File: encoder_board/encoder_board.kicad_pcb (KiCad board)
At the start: 2 copper layers, 42 x 16 mm, 8 parts, among them J1 Conn_01x06, U1 AS5048A

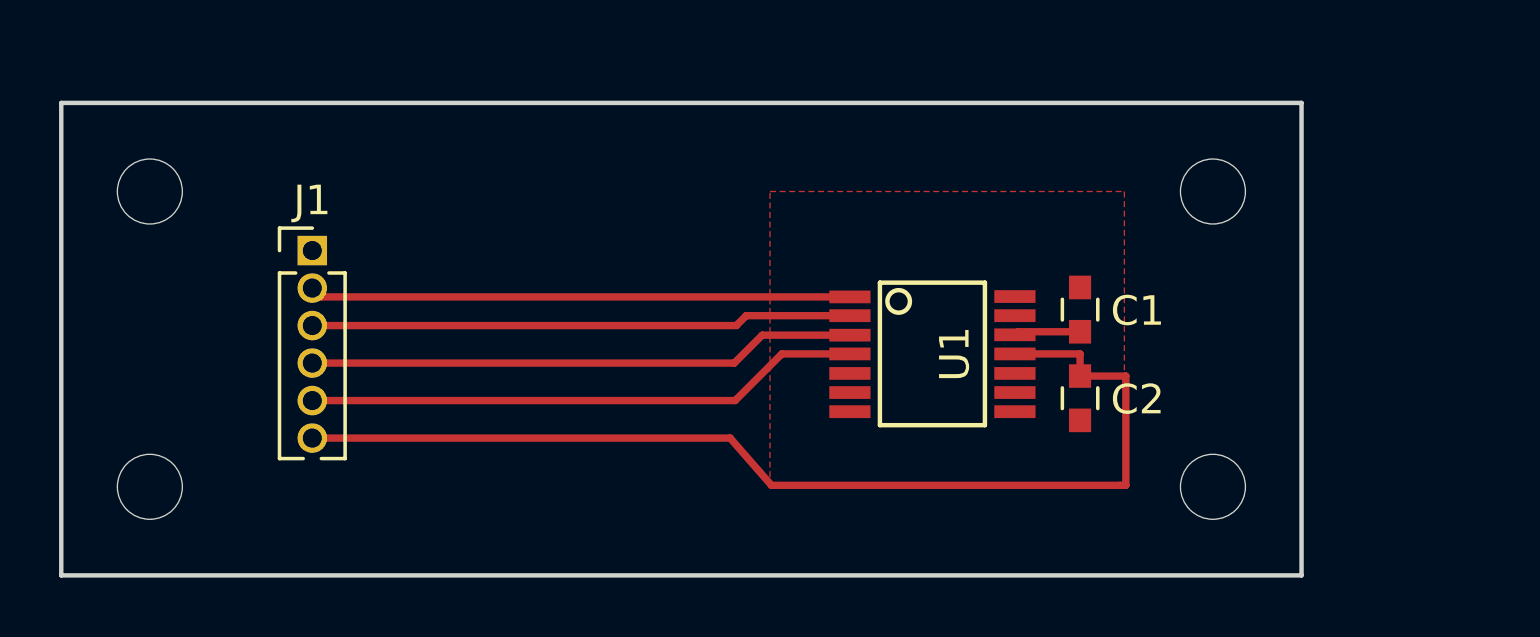
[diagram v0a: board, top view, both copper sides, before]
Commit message: add footprint for small ir sensors
 - use 0402 in encoder board
 - still need to switch sensor board
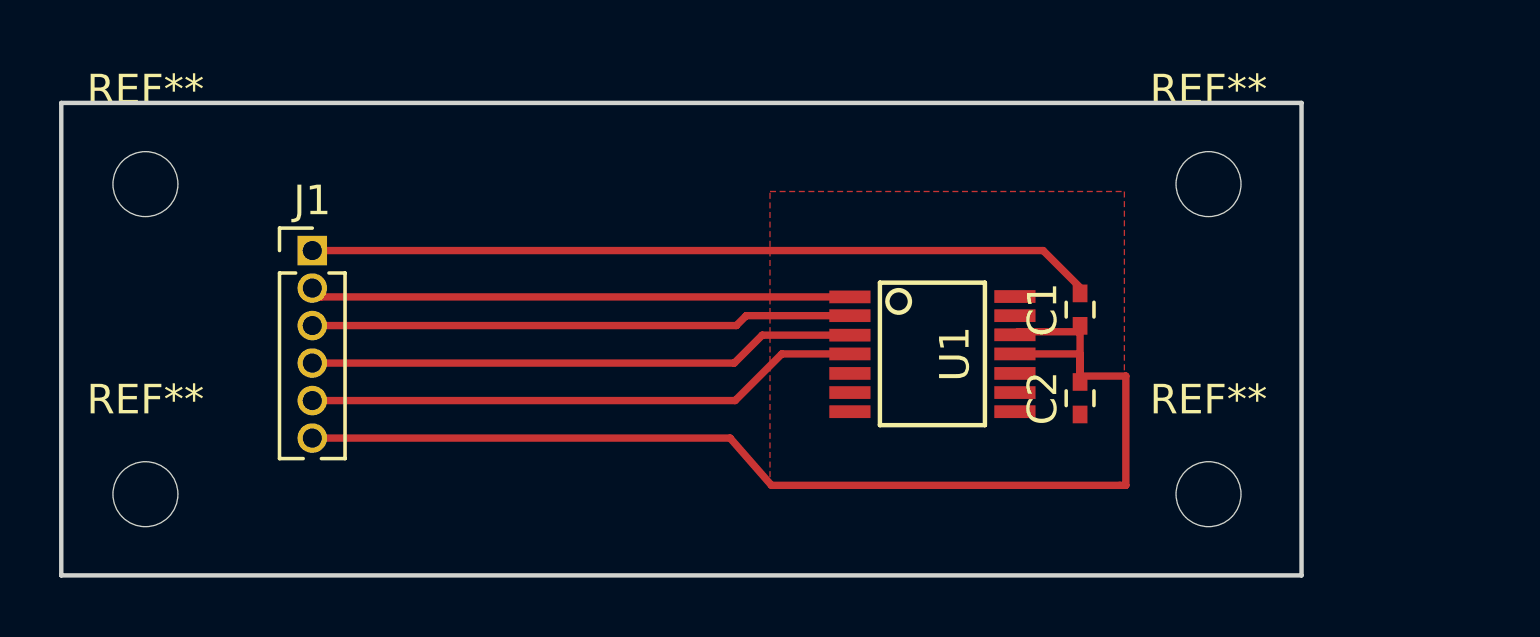
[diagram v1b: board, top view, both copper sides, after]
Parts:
- removed the REF** at (139.0, 103.0)
- removed the REF** at (139.0, 113.0)
- removed the REF** at (103.0, 103.0)
- removed the REF** at (103.0, 113.0)
- added REF**: MountingHole_2.2mm_M2, Mounting_Holes:MountingHole_2.2mm_M2, F.Cu at (102.8, 102.8)
- added REF**: MountingHole_2.2mm_M2, Mounting_Holes:MountingHole_2.2mm_M2, F.Cu at (102.8, 113.2)
- added REF**: MountingHole_2.2mm_M2, Mounting_Holes:MountingHole_2.2mm_M2, F.Cu at (138.8, 113.2)
- added REF**: MountingHole_2.2mm_M2, Mounting_Holes:MountingHole_2.2mm_M2, F.Cu at (138.8, 102.8)
- C1, C2: footprint Capacitors_SMD:C_0603 -> Capacitors_SMD:C_0402
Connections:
- C1 pad 1: Net-(C1-Pad1) -> +3V3
- C2 pad 2: +5V -> +3V3
- J1 pad 6: +5V -> +3V3
- U1 pad 11: +5V -> +3V3
- U1 pad 12: Net-(C1-Pad1) -> +3V3
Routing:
- net +3V3: track 0.00 -> 40.4 mm
- net +5V: track 36.5 -> 0.00 mm
- net GND: track 0.00 -> 26.5 mm
- net Net-(C1-Pad1): track 2.25 -> 0.00 mm

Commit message: fix grid origin and tweaked placement
 - added nice dimension indicators
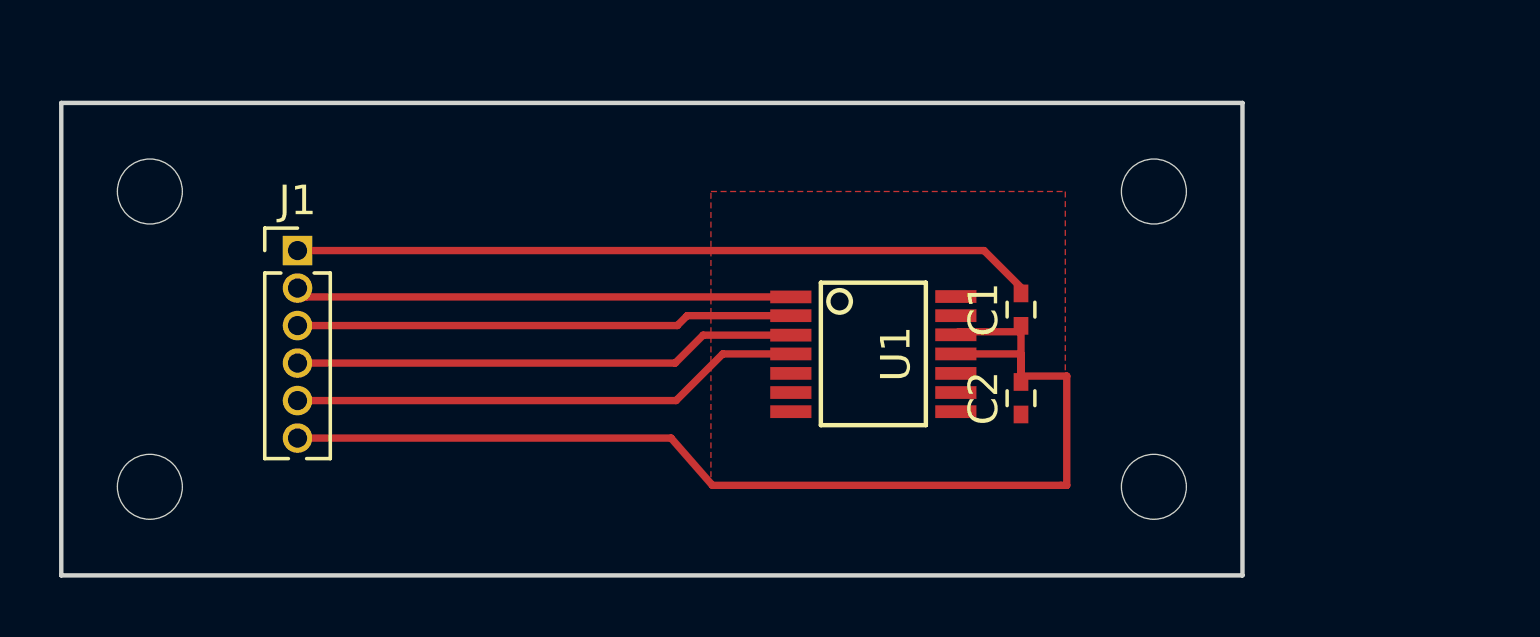
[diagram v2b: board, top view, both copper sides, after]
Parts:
- moved C1 2.00 mm to (132.5, 107.0)
- moved C2 2.00 mm to (132.5, 110.0)
- moved U1 2.00 mm to (127.5, 108.5)
- moved REF** 1.87 mm to (137.0, 113.0)
- moved REF** 1.87 mm to (137.0, 103.0)
- moved J1 0.50 mm to (108.0, 105.0)
- moved REF** 0.29 mm to (103.0, 103.0)
- moved REF** 0.29 mm to (103.0, 113.0)
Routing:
- net Net-(J1-Pad5): track 18.9 -> 17.4 mm
- net Net-(J1-Pad4): track 18.6 -> 17.1 mm
- net Net-(J1-Pad3): track 18.3 -> 16.8 mm
- net Net-(J1-Pad2): track 18.3 -> 16.8 mm
- net GND: track 26.5 -> 25.0 mm
- net +3V3: track 40.4 -> 38.9 mm
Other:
- board size 42 x 16 mm -> 40 x 16 mm

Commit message: make board symetrical and longer
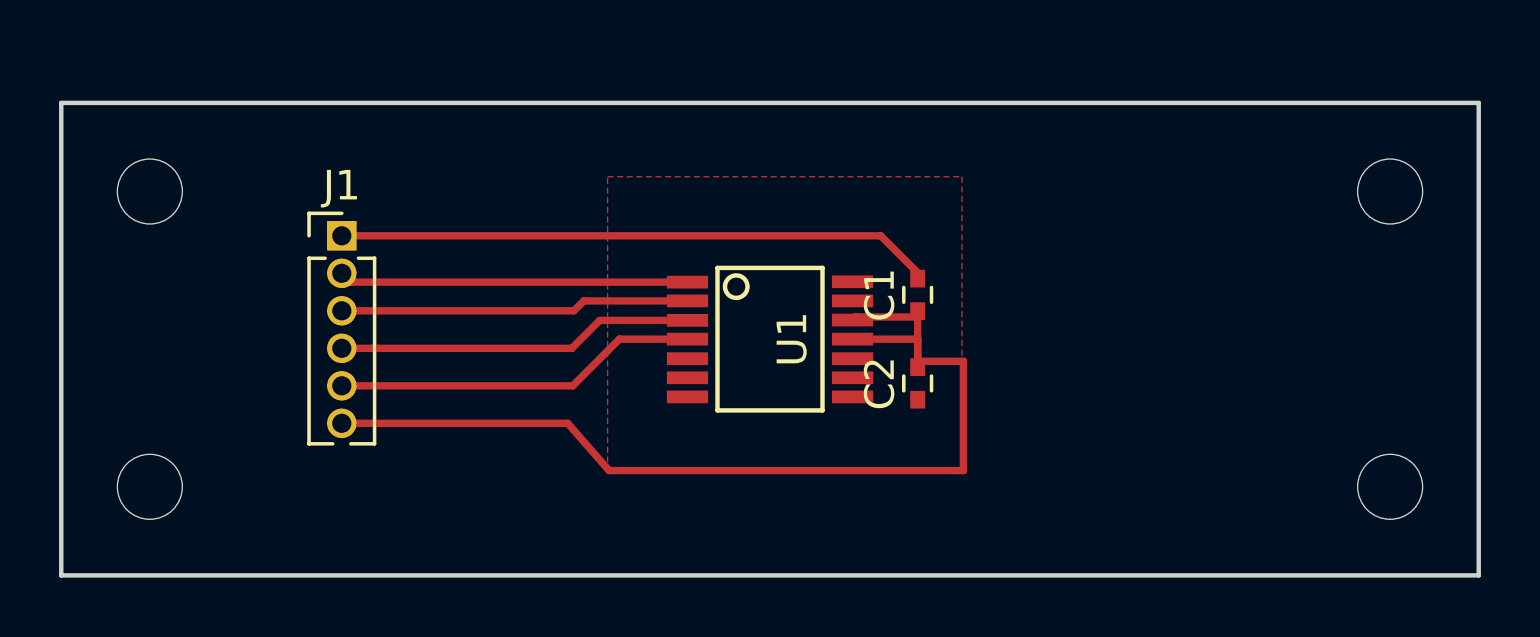
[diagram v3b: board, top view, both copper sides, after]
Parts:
- moved REF** 8.00 mm to (145.0, 113.0)
- moved REF** 8.00 mm to (145.0, 103.0)
- moved C1 3.54 mm to (129.0, 106.5)
- moved C2 3.54 mm to (129.0, 109.5)
- moved U1 3.54 mm to (124.0, 108.0)
- moved J1 1.58 mm to (109.5, 104.5)
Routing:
- net Net-(J1-Pad4): track 17.1 -> 12.1 mm
- net Net-(J1-Pad5): track 17.4 -> 12.4 mm
- net GND: track 25.0 -> 20.0 mm
- net Net-(J1-Pad3): track 16.8 -> 11.8 mm
- net Net-(J1-Pad2): track 16.8 -> 11.8 mm
- net +3V3: track 38.9 -> 33.9 mm
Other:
- board size 40 x 16 mm -> 48 x 16 mm
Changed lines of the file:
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@@
     (links 17)
     (no_connects 0)
-    (area 99.924999 99.924999 140.075001 116.075001)
+    (area 99.924999 99.924999 148.075001 116.075001)
     (thickness 1.6)
-    (drawings 8)
+    (drawings 6)
     (tracks 25)
     (zones 0)
@@
     (aux_axis_origin 0 0)
     (grid_origin 100 100)
-    (visible_elements 7FFFFFFF)
+    (visible_elements 7FFFFF7F)
     (pcbplotparams
       (layerselection 0x00030_80000001)
@@
   )
   (module Mounting_Holes:MountingHole_2.2mm_M2 (layer F.Cu)
-    (at 137 113)
+    (at 145 113)
     (descr "Mounting Hole 2.2mm, no annular, M2")
     (tags "mounting hole 2.2mm no annular m2")
@@
   )
   (module SMD_Packages:SSOP-14 (layer F.Cu)
-    (at 127.5 108.5 270)
+    (at 124 108 270)
     (attr smd)
     (fp_text reference U1 (at 0 -0.762 270) (layer F.SilkS)
@@
   )
   (module Pin_Headers:Pin_Header_Straight_1x06_Pitch1.27mm (layer F.Cu)
-    (at 108 105)
+    (at 109.5 104.5)
     (descr "Through hole straight pin header, 1x06, 1.27mm pitch, single row")
     (tags "Through hole pin header THT 1x06 1.27mm single row")
@@
   )
   (module Capacitors_SMD:C_0402 (layer F.Cu)
-    (at 132.5 107 90)
+    (at 129 106.5 90)
     (descr "Capacitor SMD 0402, reflow soldering, AVX (see smccp.pdf)")
     (tags "capacitor 0402")
@@
   )
   (module Capacitors_SMD:C_0402 (layer F.Cu)
-    (at 132.5 110 90)
+    (at 129 109.5 90)
     (descr "Capacitor SMD 0402, reflow soldering, AVX (see smccp.pdf)")
     (tags "capacitor 0402")
@@
   )
   (module Mounting_Holes:MountingHole_2.2mm_M2 (layer F.Cu)
-    (at 137 103)
+    (at 145 103)
     (descr "Mounting Hole 2.2mm, no annular, M2")
     (tags "mounting hole 2.2mm no annular m2")
@@
     (pad 1 np_thru_hole circle (at 0 0) (size 2.2 2.2) (drill 2.2) (layers *.Cu *.Mask))
   )
-  (dimension 10 (width 0.3) (layer Cmts.User)
-    (gr_text "10.000 mm" (at 90.65 108 90) (layer Cmts.User)
-      (effects (font (size 1.5 1.5) (thickness 0.3)))
-    )
-    (feature1 (pts (xy 103 103) (xy 89.3 103)))
-    (feature2 (pts (xy 103 113) (xy 89.3 113)))
-    (crossbar (pts (xy 92 113) (xy 92 103)))
-    (arrow1a (pts (xy 92 103) (xy 92.586421 104.126504)))
-    (arrow1b (pts (xy 92 103) (xy 91.413579 104.126504)))
-    (arrow2a (pts (xy 92 113) (xy 92.586421 111.873496)))
-    (arrow2b (pts (xy 92 113) (xy 91.413579 111.873496)))
-  )
-  (dimension 34 (width 0.3) (layer Cmts.User)
-    (gr_text "34.000 mm" (at 120 119.35) (layer Cmts.User)
-      (effects (font (size 1.5 1.5) (thickness 0.3)))
-    )
-    (feature1 (pts (xy 103 113) (xy 103 120.7)))
-    (feature2 (pts (xy 137 113) (xy 137 120.7)))
-    (crossbar (pts (xy 137 118) (xy 103 118)))
-    (arrow1a (pts (xy 103 118) (xy 104.126504 117.413579)))
-    (arrow1b (pts (xy 103 118) (xy 104.126504 118.586421)))
-    (arrow2a (pts (xy 137 118) (xy 135.873496 117.413579)))
-    (arrow2b (pts (xy 137 118) (xy 135.873496 118.586421)))
-  )
-  (dimension 16 (width 0.3) (layer Cmts.User)
-    (gr_text "16.000 mm" (at 149.35 108 270) (layer Cmts.User)
-      (effects (font (size 1.5 1.5) (thickness 0.3)))
-    )
-    (feature1 (pts (xy 140 116) (xy 150.7 116)))
-    (feature2 (pts (xy 140 100) (xy 150.7 100)))
-    (crossbar (pts (xy 148 100) (xy 148 116)))
-    (arrow1a (pts (xy 148 116) (xy 147.413579 114.873496)))
-    (arrow1b (pts (xy 148 116) (xy 148.586421 114.873496)))
-    (arrow2a (pts (xy 148 100) (xy 147.413579 101.126504)))
-    (arrow2b (pts (xy 148 100) (xy 148.586421 101.126504)))
-  )
-  (dimension 40 (width 0.3) (layer Cmts.User)
-    (gr_text "40.000 mm" (at 120 95.65) (layer Cmts.User)
-      (effects (font (size 1.5 1.5) (thickness 0.3)))
-    )
-    (feature1 (pts (xy 140 100) (xy 140 94.3)))
-    (feature2 (pts (xy 100 100) (xy 100 94.3)))
-    (crossbar (pts (xy 100 97) (xy 140 97)))
-    (arrow1a (pts (xy 140 97) (xy 138.873496 97.586421)))
-    (arrow1b (pts (xy 140 97) (xy 138.873496 96.413579)))
-    (arrow2a (pts (xy 100 97) (xy 101.126504 97.586421)))
-    (arrow2b (pts (xy 100 97) (xy 101.126504 96.413579)))
-  )
+  (gr_line (start 100.5 108) (end 147.5 108) (angle 90) (layer Cmts.User) (width 0.2))
+  (gr_line (start 124 100.5) (end 124 115.5) (angle 90) (layer Cmts.User) (width 0.2))
   (gr_line (start 100 116) (end 100 100) (angle 90) (layer Edge.Cuts) (width 0.15))
-  (gr_line (start 140 116) (end 100 116) (angle 90) (layer Edge.Cuts) (width 0.15))
-  (gr_line (start 140 100) (end 140 116) (angle 90) (layer Edge.Cuts) (width 0.15))
-  (gr_line (start 100 100) (end 140 100) (angle 90) (layer Edge.Cuts) (width 0.15))
-  (segment (start 108 105) (end 131.25 105) (width 0.25) (layer F.Cu) (net 1) (status 10))
-  (segment (start 131.25 105) (end 132.5 106.25) (width 0.25) (layer F.Cu) (net 1))
-  (segment (start 124.706 106.5696) (end 108.2996 106.5696) (width 0.25) (layer F.Cu) (net 2) (status 20))
-  (segment (start 108.2996 106.5696) (end 108 106.27) (width 0.25) (layer F.Cu) (net 2) (status 30))
-  (segment (start 108 107.54) (end 120.86 107.54) (width 0.25) (layer F.Cu) (net 3) (status 10))
-  (segment (start 120.86 107.54) (end 121.1954 107.2046) (width 0.25) (layer F.Cu) (net 3))
-  (segment (start 121.1954 107.2046) (end 124.706 107.2046) (width 0.25) (layer F.Cu) (net 3))
-  (segment (start 108 108.81) (end 120.79 108.81) (width 0.25) (layer F.Cu) (net 4) (status 10))
-  (segment (start 120.79 108.81) (end 121.735 107.865) (width 0.25) (layer F.Cu) (net 4))
-  (segment (start 121.735 107.865) (end 124.706 107.865) (width 0.25) (layer F.Cu) (net 4))
-  (segment (start 108 110.08) (end 120.82 110.08) (width 0.25) (layer F.Cu) (net 5) (status 10))
-  (segment (start 120.82 110.08) (end 122.4 108.5) (width 0.25) (layer F.Cu) (net 5))
-  (segment (start 122.4 108.5) (end 124.706 108.5) (width 0.25) (layer F.Cu) (net 5))
-  (segment (start 132.5 109.25) (end 134.05 109.25) (width 0.25) (layer F.Cu) (net 7))
-  (segment (start 122.05 112.95) (end 120.65 111.35) (width 0.25) (layer F.Cu) (net 7))
-  (segment (start 120.65 111.35) (end 108 111.35) (width 0.25) (layer F.Cu) (net 7) (status 20))
-  (segment (start 133.85 112.95) (end 122.05 112.95) (width 0.25) (layer F.Cu) (net 7))
-  (segment (start 134.05 112.95) (end 133.85 112.95) (width 0.25) (layer F.Cu) (net 7))
-  (segment (start 134.05 109.25) (end 134.05 112.95) (width 0.25) (layer F.Cu) (net 7))
-  (segment (start 132.5 107.75) (end 132.5 109.25) (width 0.25) (layer F.Cu) (net 7))
-  (segment (start 132.5 107.75) (end 130.3963 107.75) (width 0.25) (layer F.Cu) (net 7))
-  (segment (start 130.3963 107.75) (end 130.294 107.8523) (width 0.25) (layer F.Cu) (net 7))
-  (segment (start 132.5 109.25) (end 132.5 108.5) (width 0.25) (layer F.Cu) (net 7) (status 12))
-  (segment (start 132.5 108.5) (end 130.294 108.5) (width 0.25) (layer F.Cu) (net 7))
-  (segment (start 130.3963 107.75) (end 130.294 107.8523) (width 0.25) (layer F.Cu) (net 7))
+  (gr_line (start 148 116) (end 100 116) (angle 90) (layer Edge.Cuts) (width 0.15))
+  (gr_line (start 148 100) (end 148 116) (angle 90) (layer Edge.Cuts) (width 0.15))
+  (gr_line (start 100 100) (end 148 100) (angle 90) (layer Edge.Cuts) (width 0.15))
+  (segment (start 109.5 104.5) (end 127.75 104.5) (width 0.25) (layer F.Cu) (net 1) (status 10))
+  (segment (start 127.75 104.5) (end 129 105.75) (width 0.25) (layer F.Cu) (net 1))
+  (segment (start 121.206 106.0696) (end 109.7996 106.0696) (width 0.25) (layer F.Cu) (net 2) (status 20))
+  (segment (start 109.7996 106.0696) (end 109.5 105.77) (width 0.25) (layer F.Cu) (net 2) (status 30))
+  (segment (start 109.5 107.04) (end 117.36 107.04) (width 0.25) (layer F.Cu) (net 3) (status 10))
+  (segment (start 117.36 107.04) (end 117.6954 106.7046) (width 0.25) (layer F.Cu) (net 3))
+  (segment (start 117.6954 106.7046) (end 121.206 106.7046) (width 0.25) (layer F.Cu) (net 3))
+  (segment (start 109.5 108.31) (end 117.29 108.31) (width 0.25) (layer F.Cu) (net 4) (status 10))
+  (segment (start 117.29 108.31) (end 118.235 107.365) (width 0.25) (layer F.Cu) (net 4))
+  (segment (start 118.235 107.365) (end 121.206 107.365) (width 0.25) (layer F.Cu) (net 4))
+  (segment (start 109.5 109.58) (end 117.32 109.58) (width 0.25) (layer F.Cu) (net 5) (status 10))
+  (segment (start 117.32 109.58) (end 118.9 108) (width 0.25) (layer F.Cu) (net 5))
+  (segment (start 118.9 108) (end 121.206 108) (width 0.25) (layer F.Cu) (net 5))
+  (segment (start 129 108.75) (end 130.55 108.75) (width 0.25) (layer F.Cu) (net 7))
+  (segment (start 118.55 112.45) (end 117.15 110.85) (width 0.25) (layer F.Cu) (net 7))
+  (segment (start 117.15 110.85) (end 109.5 110.85) (width 0.25) (layer F.Cu) (net 7) (status 20))
+  (segment (start 130.35 112.45) (end 118.55 112.45) (width 0.25) (layer F.Cu) (net 7))
+  (segment (start 130.55 112.45) (end 130.35 112.45) (width 0.25) (layer F.Cu) (net 7))
+  (segment (start 130.55 108.75) (end 130.55 112.45) (width 0.25) (layer F.Cu) (net 7))
+  (segment (start 129 107.25) (end 129 108.75) (width 0.25) (layer F.Cu) (net 7))
+  (segment (start 129 107.25) (end 126.8963 107.25) (width 0.25) (layer F.Cu) (net 7))
+  (segment (start 126.8963 107.25) (end 126.794 107.3523) (width 0.25) (layer F.Cu) (net 7))
+  (segment (start 129 108.75) (end 129 108) (width 0.25) (layer F.Cu) (net 7) (status 12))
+  (segment (start 129 108) (end 126.794 108) (width 0.25) (layer F.Cu) (net 7))
+  (segment (start 126.8963 107.25) (end 126.794 107.3523) (width 0.25) (layer F.Cu) (net 7))
   (zone (net 1) (net_name GND) (layer F.Cu) (hatch edge 0.508)
     (connect_pads (clearance 0.25))
@@
     (polygon
       (pts
-        (xy 134 113) (xy 122 113) (xy 122 103) (xy 134 103)
+        (xy 130.5 112.5) (xy 118.5 112.5) (xy 118.5 102.5) (xy 130.5 102.5)
       )
     )

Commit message: use named nets
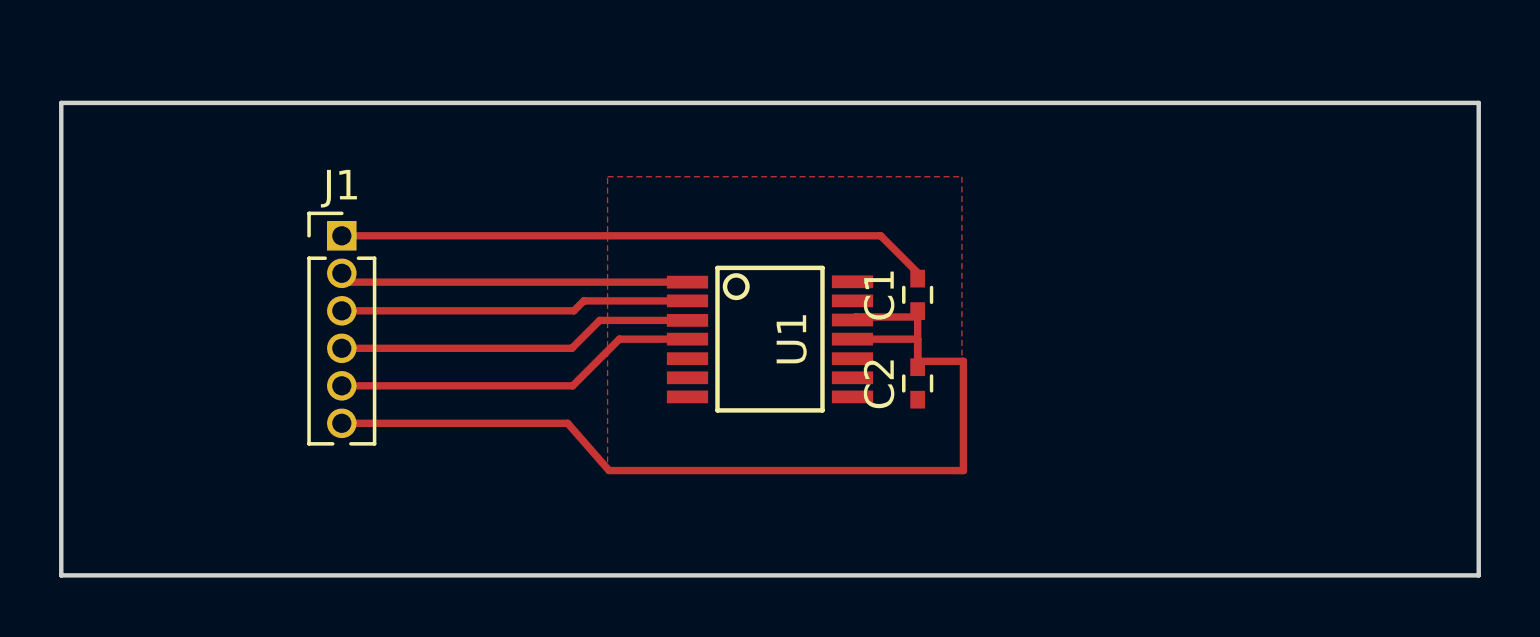
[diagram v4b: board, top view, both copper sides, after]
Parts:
- removed REF** (x4): MountingHole_2.2mm_M2, Mounting_Holes:MountingHole_2.2mm_M2
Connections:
- net Net-(J1-Pad2) renamed CS
- net Net-(J1-Pad3) renamed CLK
- net Net-(J1-Pad4) renamed MISO
- net Net-(J1-Pad5) renamed MOSI
